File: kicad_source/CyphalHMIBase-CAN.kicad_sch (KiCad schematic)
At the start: 27 parts, among them CN1 RASPBERRYPI_PICO, CN2 SM04B-SRSS-TB, CN3 SM04B-SRSS-TB, CN7 DNI, SW1 PTS636 SM43 SMTR LFS, U3 M24C64-RMN6TP

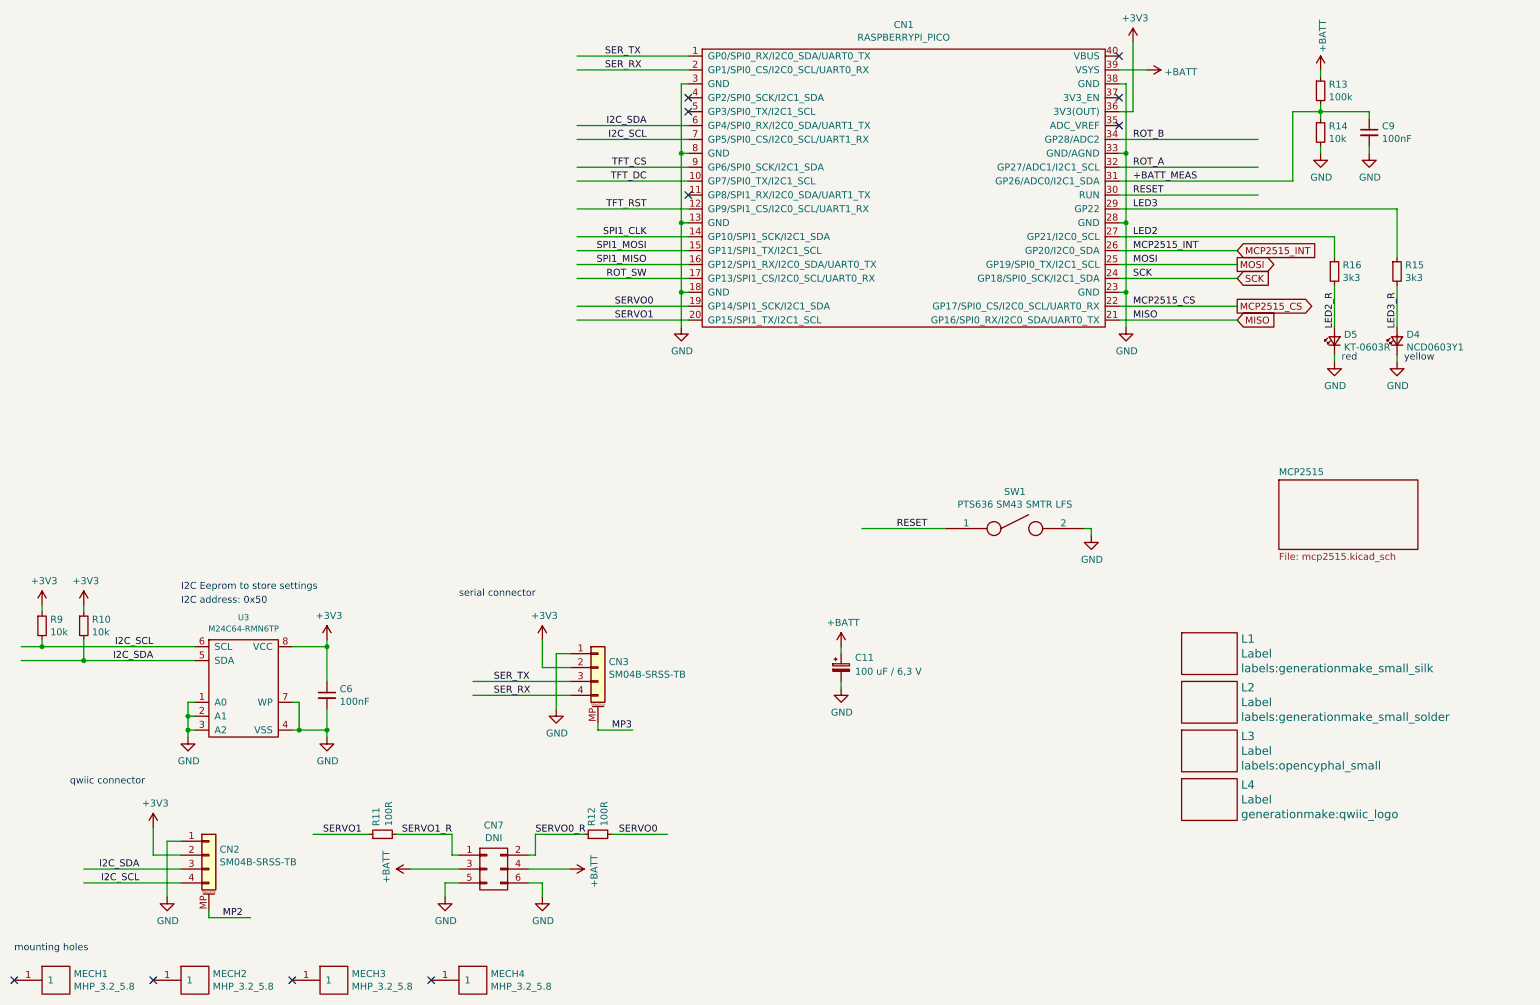
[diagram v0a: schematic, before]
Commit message: added display
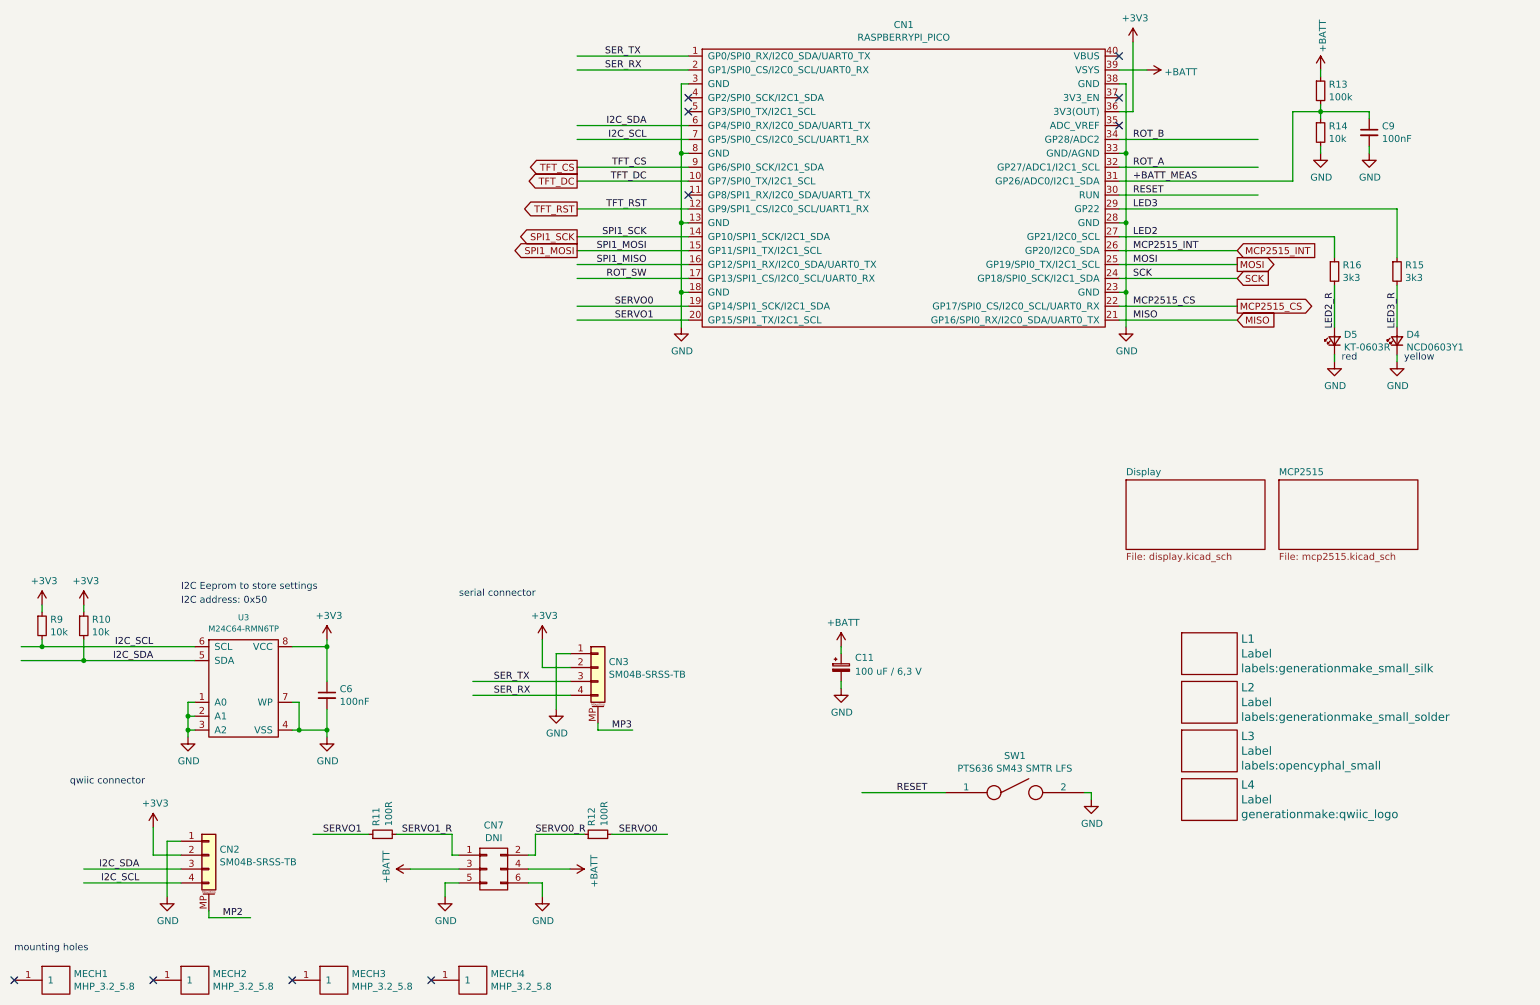
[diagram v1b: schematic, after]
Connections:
- net SPI1_CLK renamed SPI1_SCK
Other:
- added sheet Display (display.kicad_sch)
- moved on the sheet: SW1
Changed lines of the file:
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@@
 	(wire
 		(pts
-			(xy 172.72 110.49) (xy 187.96 110.49)
+			(xy 172.72 158.75) (xy 187.96 158.75)
 		)
 		(stroke
@@
 	(wire
 		(pts
-			(xy 214.63 110.49) (xy 214.63 111.76)
+			(xy 214.63 158.75) (xy 214.63 160.02)
 		)
 		(stroke
@@
 	(wire
 		(pts
-			(xy 213.36 110.49) (xy 214.63 110.49)
+			(xy 213.36 158.75) (xy 214.63 158.75)
 		)
 		(stroke
@@
 	)
 	(label "RESET"
-		(at 179.07 110.49 0)
+		(at 179.07 158.75 0)
 		(effects
 			(font
@@
 		)
 	)
-	(label "SPI1_CLK"
+	(label "SPI1_SCK"
 		(at 133.35 57.15 180)
 		(effects
@@
 		)
 	)
+	(global_label "SPI1_SCK"
+		(shape output)
+		(at 120.65 57.15 180)
+		(fields_autoplaced yes)
+		(effects
+			(font
+				(size 1.27 1.27)
+			)
+			(justify right)
+		)
+		(property "Intersheetrefs" "${INTERSHEET_REFS}"
+			(at 109.3081 57.15 0)
+			(effects
+				(font
+					(size 1.27 1.27)
+				)
+				(justify right)
+				(hide yes)
+			)
+		)
+		(property "Referenzen zwischen Schaltplänen" "${INTERSHEET_REFS}"
+			(at 120.65 58.9852 0)
+			(effects
+				(font
+					(size 1.27 1.27)
+				)
+				(justify right)
+				(hide yes)
+			)
+		)
+	)
+	(global_label "TFT_RST"
+		(shape output)
+		(at 120.65 52.07 180)
+		(fields_autoplaced yes)
+		(effects
+			(font
+				(size 1.27 1.27)
+			)
+			(justify right)
+		)
+		(property "Intersheetrefs" "${INTERSHEET_REFS}"
+			(at 110.8805 52.07 0)
+			(effects
+				(font
+					(size 1.27 1.27)
+				)
+				(justify right)
+				(hide yes)
+			)
+		)
+		(property "Referenzen zwischen Schaltplänen" "${INTERSHEET_REFS}"
+			(at 120.65 53.9052 0)
+			(effects
+				(font
+					(size 1.27 1.27)
+				)
+				(justify right)
+				(hide yes)
+			)
+		)
+	)
+	(global_label "TFT_DC"
+		(shape output)
+		(at 120.65 46.99 180)
+		(fields_autoplaced yes)
+		(effects
+			(font
+				(size 1.27 1.27)
+			)
+			(justify right)
+		)
+		(property "Intersheetrefs" "${INTERSHEET_REFS}"
+			(at 111.7876 46.99 0)
+			(effects
+				(font
+					(size 1.27 1.27)
+				)
+				(justify right)
+				(hide yes)
+			)
+		)
+		(property "Referenzen zwischen Schaltplänen" "${INTERSHEET_REFS}"
+			(at 120.65 48.8252 0)
+			(effects
+				(font
+					(size 1.27 1.27)
+				)
+				(justify right)
+				(hide yes)
+			)
+		)
+	)
 	(global_label "MOSI"
 		(shape output)
@@
 		)
 	)
+	(global_label "SPI1_MOSI"
+		(shape output)
+		(at 120.65 59.69 180)
+		(fields_autoplaced yes)
+		(effects
+			(font
+				(size 1.27 1.27)
+			)
+			(justify right)
+		)
+		(property "Intersheetrefs" "${INTERSHEET_REFS}"
+			(at 108.4614 59.69 0)
+			(effects
+				(font
+					(size 1.27 1.27)
+				)
+				(justify right)
+				(hide yes)
+			)
+		)
+		(property "Referenzen zwischen Schaltplänen" "${INTERSHEET_REFS}"
+			(at 120.65 61.5252 0)
+			(effects
+				(font
+					(size 1.27 1.27)
+				)
+				(justify right)
+				(hide yes)
+			)
+		)
+	)
+	(global_label "TFT_CS"
+		(shape output)
+		(at 120.65 44.45 180)
+		(fields_autoplaced yes)
+		(effects
+			(font
+				(size 1.27 1.27)
+			)
+			(justify right)
+		)
+		(property "Intersheetrefs" "${INTERSHEET_REFS}"
+			(at 111.8481 44.45 0)
+			(effects
+				(font
+					(size 1.27 1.27)
+				)
+				(justify right)
+				(hide yes)
+			)
+		)
+		(property "Referenzen zwischen Schaltplänen" "${INTERSHEET_REFS}"
+			(at 120.65 46.2852 0)
+			(effects
+				(font
+					(size 1.27 1.27)
+				)
+				(justify right)
+				(hide yes)
+			)
+		)
+	)
 	(global_label "SCK"
 		(shape input)
@@
 	(symbol
 		(lib_id "OpenCyphalPicoBase-rescue:SPST-devices")
-		(at 200.66 110.49 0)
+		(at 200.66 158.75 0)
 		(unit 1)
 		(exclude_from_sim no)
@@
 		(dnp no)
 		(property "Reference" "SW1"
-			(at 200.66 103.759 0)
+			(at 200.66 152.019 0)
 			(effects
 				(font
@@
 		)
 		(property "Value" "PTS636 SM43 SMTR LFS"
-			(at 200.66 106.0704 0)
+			(at 200.66 154.3304 0)
 			(effects
 				(font
@@
 		)
 		(property "Footprint" "Button_Switch_SMD:SW_SPST_CK_RS282G05A3"
-			(at 200.66 110.49 0)
+			(at 200.66 158.75 0)
 			(effects
 				(font
@@
 		)
 		(property "Datasheet" ""
-			(at 200.66 110.49 0)
+			(at 200.66 158.75 0)
 			(effects
 				(font
@@
 		)
 		(property "Description" ""
-			(at 200.66 110.49 0)
+			(at 200.66 158.75 0)
 			(effects
 				(font
@@
 		)
 		(property "LCSC" "C2800965"
-			(at 200.66 110.49 0)
+			(at 200.66 158.75 0)
 			(effects
 				(font
@@
 	(symbol
 		(lib_id "OpenCyphalPicoBase-rescue:GND-power-supply")
-		(at 214.63 111.76 0)
+		(at 214.63 160.02 0)
 		(unit 1)
 		(exclude_from_sim no)
@@
 		(dnp no)
 		(property "Reference" "#PWR054"
-			(at 214.63 118.11 0)
+			(at 214.63 166.37 0)
 			(effects
 				(font
@@
 		)
 		(property "Value" "GND"
-			(at 214.757 116.1542 0)
+			(at 214.757 164.4142 0)
 			(effects
 				(font
@@
 		)
 		(property "Footprint" ""
-			(at 214.63 111.76 0)
+			(at 214.63 160.02 0)
 			(effects
 				(font
@@
 		)
 		(property "Datasheet" ""
-			(at 214.63 111.76 0)
+			(at 214.63 160.02 0)
 			(effects
 				(font
@@
 		)
 		(property "Description" ""
-			(at 214.63 111.76 0)
+			(at 214.63 160.02 0)
 			(effects
 				(font
@@
 				)
 			)
+		)
+	)
+	(sheet
+		(at 220.98 101.6)
+		(size 25.4 12.7)
+		(fields_autoplaced yes)
+		(stroke
+			(width 0)
+			(type solid)
+		)
+		(fill
+			(color 0 0 0 0.0000)
+		)
+		(property "Sheetname" "Display"
+			(at 220.98 100.8884 0)
+			(effects
+				(font
+					(size 1.27 1.27)
+				)
+				(justify left bottom)
+			)
+		)
+		(property "Sheetfile" "display.kicad_sch"
+			(at 220.98 114.8846 0)
+			(effects
+				(font
+					(size 1.27 1.27)
+				)
+				(justify left top)
+			)
+		)
+		(instances
+			(project "CyphalHMIBase-CAN"
+				(path "/9d6d512e-1439-4aa2-b0d9-afb2dddd9146"
+					(page "3")
+				)
+			)

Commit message: added encoder, mounting holes for display at correct position
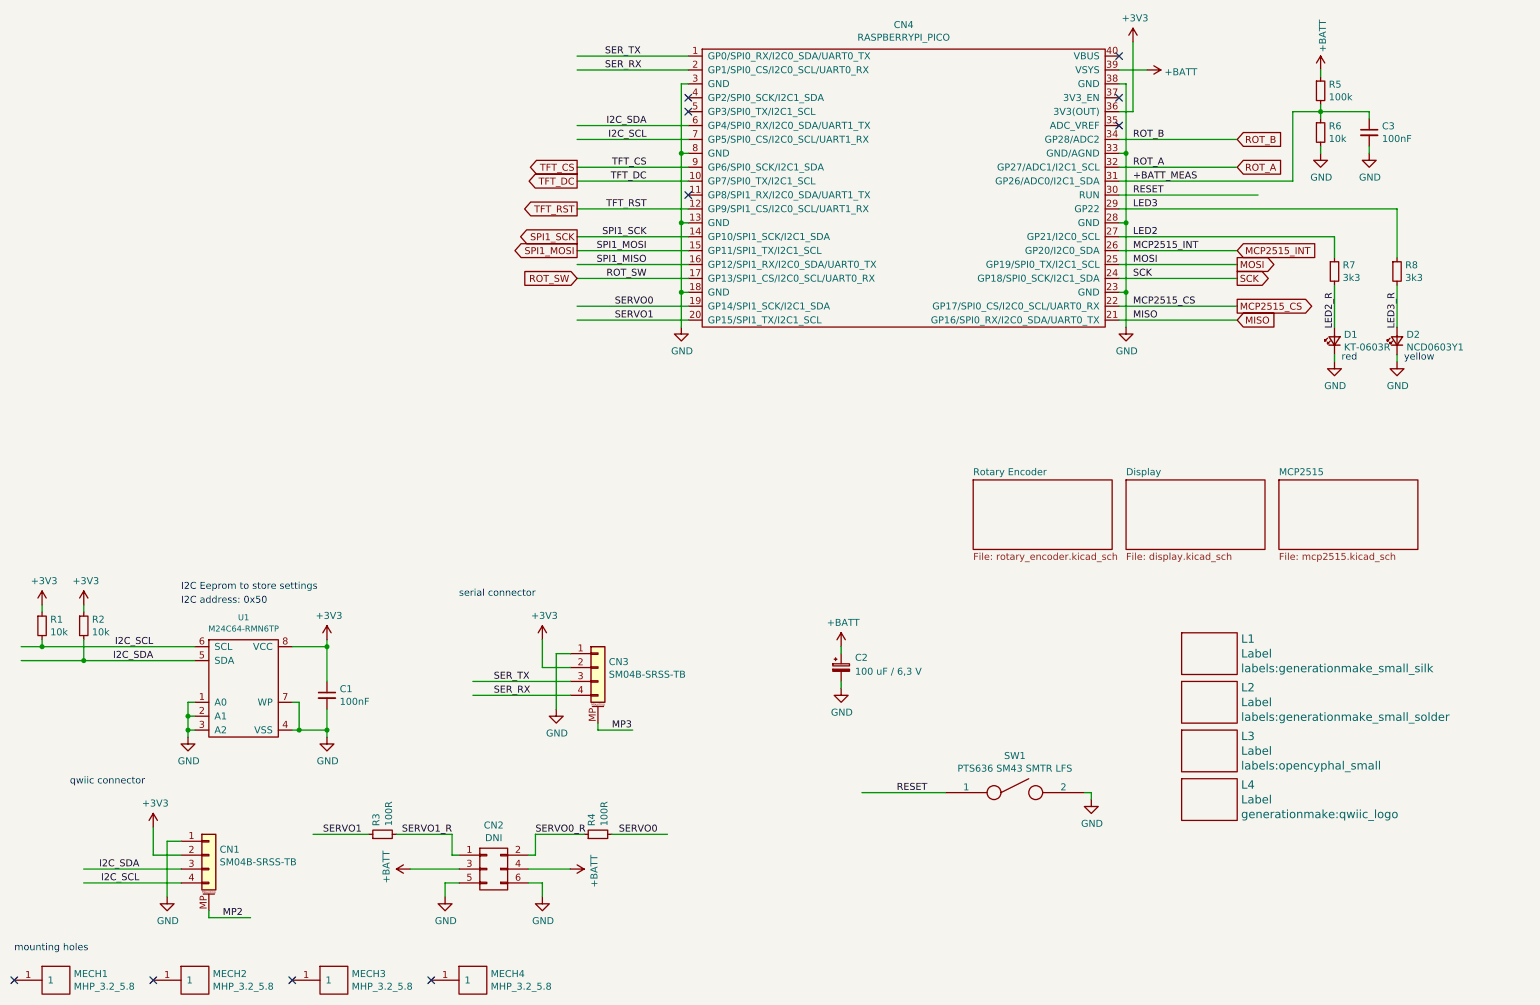
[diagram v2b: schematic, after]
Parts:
- renumbered C6 to C1, C11 to C2, C9 to C3, CN2 to CN1, CN7 to CN2, CN1 to CN4, D5 to D1, D4 to D2, R9 to R1, R10 to R2, R11 to R3, R12 to R4, R13 to R5, R14 to R6, R16 to R7, R15 to R8, U3 to U1
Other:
- added sheet Rotary Encoder (rotary_encoder.kicad_sch)

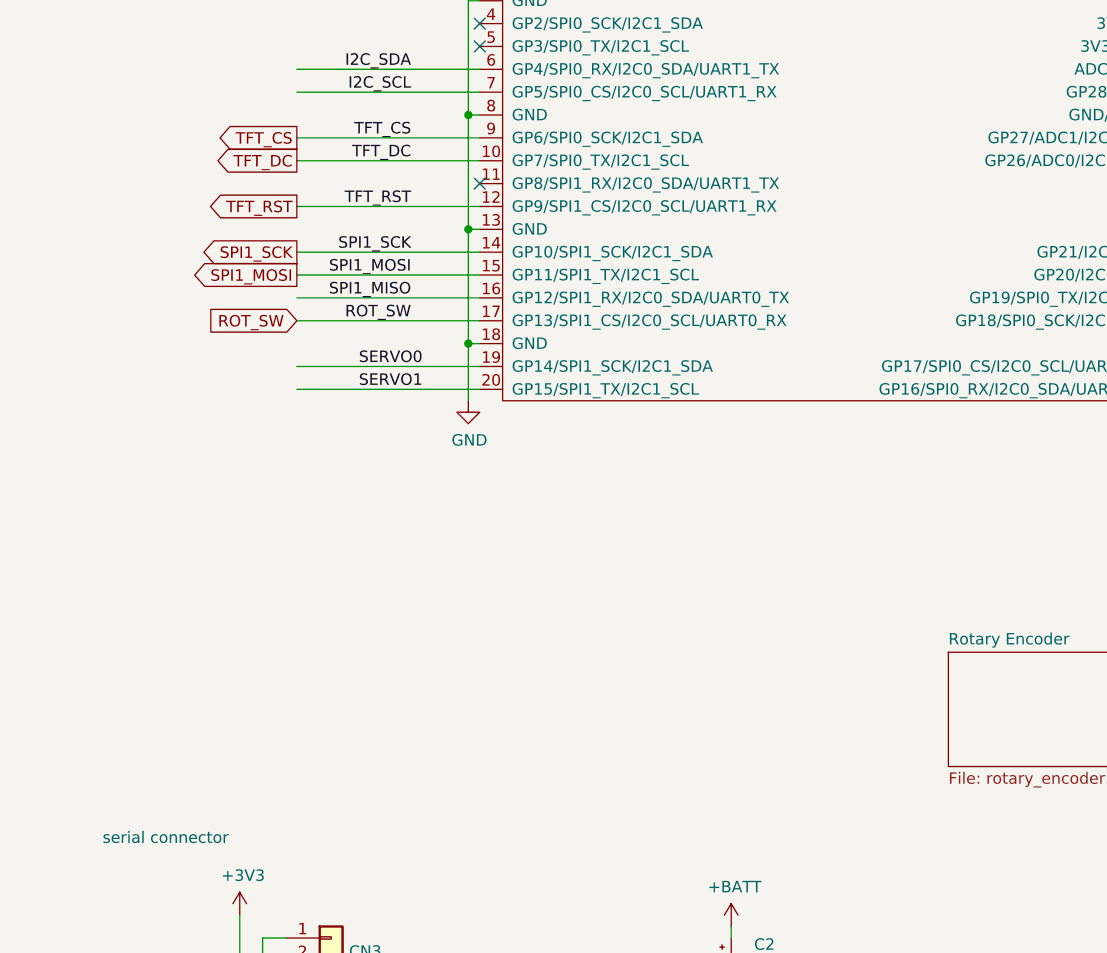
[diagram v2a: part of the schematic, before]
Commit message: added sd card, updated layout
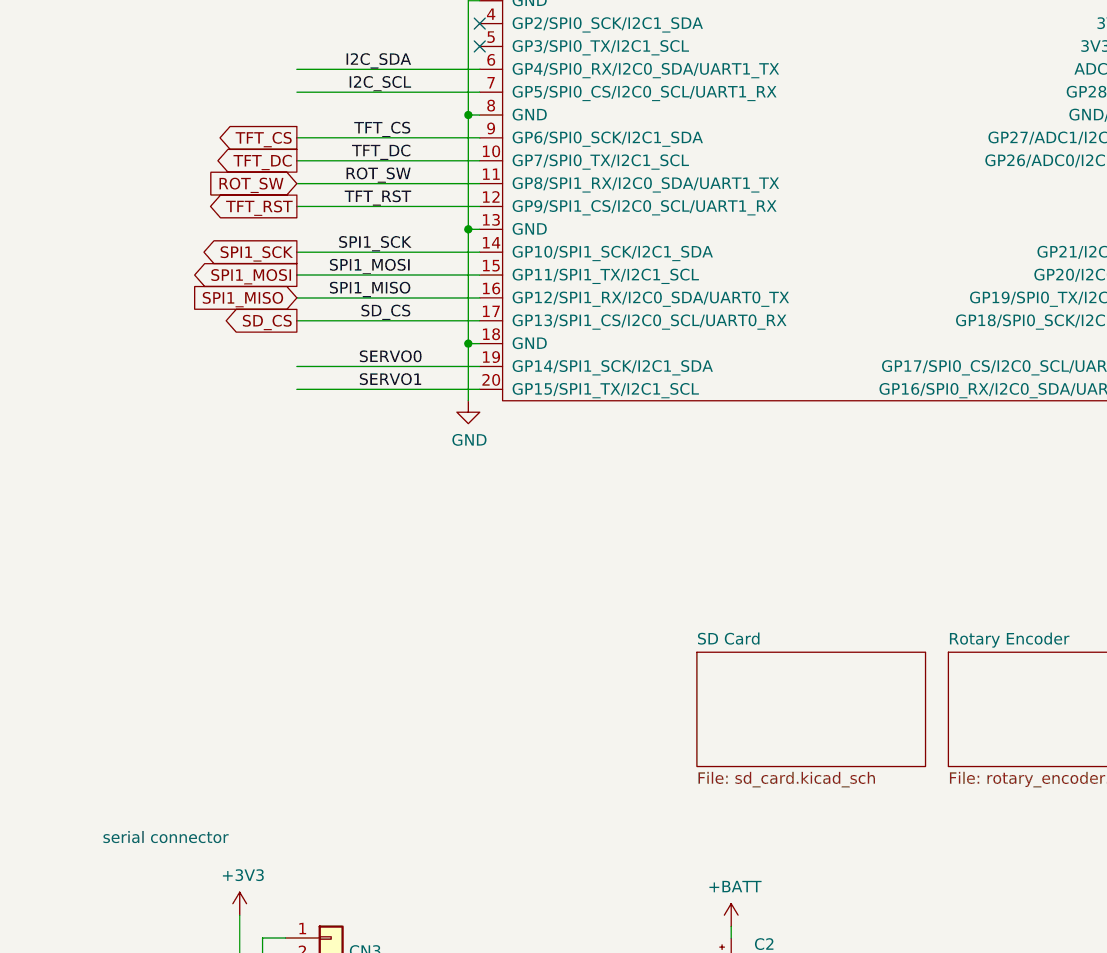
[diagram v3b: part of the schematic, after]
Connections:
- net ROT_SW: now also CN4.11 (GP8/SPI1_RX/I2C0_SDA/UART1_TX); no longer CN4.17 (GP13/SPI1_CS/I2C0_SCL/UART0_RX)
- new net SD_CS: CN4.17 (GP13/SPI1_CS/I2C0_SCL/UART0_RX)
- no-connect marks 10 -> 9
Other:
- added sheet SD Card (sd_card.kicad_sch)
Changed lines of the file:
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@@
 	(title_block
 		(title "CyphalIMUBase/CAN")
-		(date "2026-06-03")
+		(date "2026-06-05")
 		(rev "0.1")
 		(company "generationmake")
@@
 	)
 	(no_connect
-		(at 140.97 49.53)
-	)
-	(no_connect
 		(at 140.97 31.75)
 	)
@@
 	(wire
 		(pts
+			(xy 120.65 49.53) (xy 140.97 49.53)
+		)
+		(stroke
+			(width 0)
+			(type default)
+		)
+	)
+	(wire
+		(pts
 			(xy 130.81 147.32) (xy 124.46 147.32)
 		)
@@
 		)
 	)
+	(label "SD_CS"
+		(at 133.35 64.77 180)
+		(effects
+			(font
+				(size 1.27 1.27)
+			)
+			(justify right bottom)
+		)
+	)
 	(label "I2C_SCL"
 		(at 40.64 175.26 180)
@@
 	)
 	(label "ROT_SW"
-		(at 133.35 64.77 180)
+		(at 133.35 49.53 180)
 		(effects
 			(font
@@
 	(global_label "ROT_SW"
 		(shape input)
+		(at 120.65 49.53 180)
+		(fields_autoplaced yes)
+		(effects
+			(font
+				(size 1.27 1.27)
+			)
+			(justify right)
+		)
+		(property "Intersheetrefs" "${INTERSHEET_REFS}"
+			(at 111.1224 49.53 0)
+			(effects
+				(font
+					(size 1.27 1.27)
+				)
+				(justify right)
+				(hide yes)
+			)
+		)
+		(property "Referenzen zwischen Schaltplänen" "${INTERSHEET_REFS}"
+			(at 120.65 51.3652 0)
+			(effects
+				(font
+					(size 1.27 1.27)
+				)
+				(justify right)
+				(hide yes)
+			)
+		)
+	)
+	(global_label "SPI1_MISO"
+		(shape input)
+		(at 120.65 62.23 180)
+		(fields_autoplaced yes)
+		(effects
+			(font
+				(size 1.27 1.27)
+			)
+			(justify right)
+		)
+		(property "Intersheetrefs" "${INTERSHEET_REFS}"
+			(at 108.4614 62.23 0)
+			(effects
+				(font
+					(size 1.27 1.27)
+				)
+				(justify right)
+				(hide yes)
+			)
+		)
+		(property "Referenzen zwischen Schaltplänen" "${INTERSHEET_REFS}"
+			(at 120.65 64.0652 0)
+			(effects
+				(font
+					(size 1.27 1.27)
+				)
+				(justify right)
+				(hide yes)
+			)
+		)
+	)
+	(global_label "SD_CS"
+		(shape output)
 		(at 120.65 64.77 180)
 		(fields_autoplaced yes)
@@
 		)
 		(property "Intersheetrefs" "${INTERSHEET_REFS}"
-			(at 111.1224 64.77 0)
+			(at 112.3924 64.77 0)
 			(effects
 				(font
@@
 				)
 			)
+		)
+	)
+	(sheet
+		(at 165.1 101.6)
+		(size 25.4 12.7)
+		(fields_autoplaced yes)
+		(stroke
+			(width 0)
+			(type solid)
+		)
+		(fill
+			(color 0 0 0 0.0000)
+		)
+		(property "Sheetname" "SD Card"
+			(at 165.1 100.8884 0)
+			(effects
+				(font
+					(size 1.27 1.27)
+				)
+				(justify left bottom)
+			)
+		)
+		(property "Sheetfile" "sd_card.kicad_sch"
+			(at 165.1 114.8846 0)
+			(effects
+				(font
+					(size 1.27 1.27)
+				)
+				(justify left top)
+			)
+		)
+		(instances
+			(project "CyphalHMIBase-CAN"
+				(path "/9d6d512e-1439-4aa2-b0d9-afb2dddd9146"
+					(page "5")
+				)
+			)
